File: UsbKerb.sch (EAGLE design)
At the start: 21 parts, among them IC1 XMEGA16A4A

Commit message: board Layout complete?
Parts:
- added C8: 470uf, rcl:CPOL-USG
- added U1: UA78M33CDCY, usb:UA78M33CDCY
- renumbered U$1 to U2
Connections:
- removed net N$15: JP2.3
- net +3V3: now also U1.INPUT
- net +5V: now also C8.+, U1.OUTPUT
- net GND: now also C8.-, U1.COM, U1.COM_2
- net N$18: now also JP2.3
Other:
- moved on the sheet: JP2
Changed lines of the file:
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@@
 <part name="U$3" library="usb" deviceset="TVS" device=""/>
 <part name="U$4" library="usb" deviceset="12MHZ" device=""/>
-<part name="U$1" library="usb" deviceset="3.3TVS" device=""/>
+<part name="U2" library="usb" deviceset="3.3TVS" device=""/>
 <part name="GND10" library="supply1" deviceset="GND" device=""/>
 <part name="C4" library="rcl" deviceset="C-EU" device="C0805K" value="18pf"/>
@@
 <part name="+3V4" library="supply1" deviceset="+3V3" device=""/>
 <part name="+3V5" library="supply1" deviceset="+3V3" device=""/>
+<part name="U1" library="usb" deviceset="UA78M33CDCY" device=""/>
+<part name="P+3" library="supply1" deviceset="+5V" device=""/>
+<part name="GND13" library="supply1" deviceset="GND" device=""/>
+<part name="C8" library="rcl" deviceset="CPOL-US" device="G" value="470uf"/>
 </parts>
 <sheets>
@@
 <instance part="U$3" gate="G$1" x="195.58" y="-15.24"/>
 <instance part="U$4" gate="G$1" x="15.24" y="30.48" rot="R90"/>
-<instance part="U$1" gate="G$1" x="99.06" y="-22.86"/>
+<instance part="U2" gate="G$1" x="99.06" y="-22.86"/>
 <instance part="GND10" gate="1" x="195.58" y="-27.94"/>
 <instance part="C4" gate="G$1" x="2.54" y="38.1" rot="R90"/>
@@
 <instance part="C6" gate="G$1" x="210.82" y="-12.7"/>
 <instance part="C7" gate="G$1" x="220.98" y="-12.7"/>
-<instance part="JP2" gate="A" x="48.26" y="-22.86"/>
+<instance part="JP2" gate="A" x="45.72" y="-22.86"/>
 <instance part="P+8" gate="1" x="35.56" y="-12.7"/>
 <instance part="GND12" gate="1" x="63.5" y="-15.24"/>
@@
 <instance part="+3V4" gate="G$1" x="81.28" y="-12.7"/>
 <instance part="+3V5" gate="G$1" x="25.4" y="71.12"/>
+<instance part="U1" gate="A" x="251.46" y="-7.62"/>
+<instance part="P+3" gate="1" x="297.18" y="-2.54"/>
+<instance part="GND13" gate="1" x="297.18" y="-27.94"/>
+<instance part="C8" gate="G$1" x="281.94" y="-12.7"/>
 </instances>
 <busses>
@@
 <wire x1="127" y1="-20.32" x2="127" y2="25.4" width="0.1524" layer="91"/>
 <junction x="127" y="25.4"/>
-<pinref part="U$1" gate="G$1" pin="2"/>
+<pinref part="U2" gate="G$1" pin="2"/>
 <wire x1="127" y1="-20.32" x2="111.76" y2="-20.32" width="0.1524" layer="91"/>
 </segment>
@@
 <wire x1="116.84" y1="-15.24" x2="116.84" y2="20.32" width="0.1524" layer="91"/>
 <junction x="116.84" y="20.32"/>
-<pinref part="U$1" gate="G$1" pin="1"/>
+<pinref part="U2" gate="G$1" pin="1"/>
 <wire x1="116.84" y1="-15.24" x2="111.76" y2="-15.24" width="0.1524" layer="91"/>
 </segment>
@@
 <wire x1="86.36" y1="-25.4" x2="81.28" y2="-25.4" width="0.1524" layer="91"/>
 <wire x1="81.28" y1="-25.4" x2="81.28" y2="-30.48" width="0.1524" layer="91"/>
-<pinref part="U$1" gate="G$1" pin="GND"/>
+<pinref part="U2" gate="G$1" pin="GND"/>
 </segment>
 <segment>
@@
 <wire x1="210.82" y1="-17.78" x2="210.82" y2="-22.86" width="0.1524" layer="91"/>
 <junction x="210.82" y="-22.86"/>
+<pinref part="U1" gate="A" pin="COM"/>
+<wire x1="220.98" y1="-22.86" x2="251.46" y2="-22.86" width="0.1524" layer="91"/>
+<wire x1="251.46" y1="-22.86" x2="254" y2="-22.86" width="0.1524" layer="91"/>
+<wire x1="254" y1="-22.86" x2="254" y2="-17.78" width="0.1524" layer="91"/>
+<junction x="220.98" y="-22.86"/>
+<pinref part="U1" gate="A" pin="COM_2"/>
+<wire x1="251.46" y1="-17.78" x2="251.46" y2="-22.86" width="0.1524" layer="91"/>
+<junction x="251.46" y="-22.86"/>
+<wire x1="254" y1="-22.86" x2="281.94" y2="-22.86" width="0.1524" layer="91"/>
+<wire x1="281.94" y1="-22.86" x2="297.18" y2="-22.86" width="0.1524" layer="91"/>
+<wire x1="297.18" y1="-22.86" x2="297.18" y2="-25.4" width="0.1524" layer="91"/>
+<junction x="254" y="-22.86"/>
+<pinref part="GND13" gate="1" pin="GND"/>
+<pinref part="C8" gate="G$1" pin="-"/>
+<wire x1="281.94" y1="-17.78" x2="281.94" y2="-22.86" width="0.1524" layer="91"/>
+<junction x="281.94" y="-22.86"/>
 </segment>
 <segment>
@@
 <segment>
 <pinref part="JP2" gate="A" pin="2"/>
-<wire x1="53.34" y1="-20.32" x2="58.42" y2="-20.32" width="0.1524" layer="91"/>
+<wire x1="50.8" y1="-20.32" x2="58.42" y2="-20.32" width="0.1524" layer="91"/>
 <wire x1="58.42" y1="-20.32" x2="58.42" y2="-12.7" width="0.1524" layer="91"/>
 <pinref part="GND12" gate="1" pin="GND"/>
@@
 <pinref part="JP2" gate="A" pin="1"/>
 <pinref part="P+8" gate="1" pin="+5V"/>
-<wire x1="45.72" y1="-20.32" x2="35.56" y2="-20.32" width="0.1524" layer="91"/>
+<wire x1="43.18" y1="-20.32" x2="35.56" y2="-20.32" width="0.1524" layer="91"/>
 <wire x1="35.56" y1="-20.32" x2="35.56" y2="-15.24" width="0.1524" layer="91"/>
+</segment>
+<segment>
+<pinref part="U1" gate="A" pin="OUTPUT"/>
+<pinref part="P+3" gate="1" pin="+5V"/>
+<wire x1="276.86" y1="-7.62" x2="281.94" y2="-7.62" width="0.1524" layer="91"/>
+<wire x1="281.94" y1="-7.62" x2="297.18" y2="-7.62" width="0.1524" layer="91"/>
+<wire x1="297.18" y1="-7.62" x2="297.18" y2="-5.08" width="0.1524" layer="91"/>
+<pinref part="C8" gate="G$1" pin="+"/>
+<wire x1="281.94" y1="-10.16" x2="281.94" y2="-7.62" width="0.1524" layer="91"/>
+<junction x="281.94" y="-7.62"/>
 </segment>
 </net>
@@
 <wire x1="22.86" y1="5.08" x2="22.86" y2="-25.4" width="0.1524" layer="91"/>
 <pinref part="JP2" gate="A" pin="5"/>
-<wire x1="22.86" y1="-25.4" x2="45.72" y2="-25.4" width="0.1524" layer="91"/>
+<wire x1="22.86" y1="-25.4" x2="43.18" y2="-25.4" width="0.1524" layer="91"/>
 </segment>
 </net>
 <net name="N$18" class="0">
 <segment>
-<pinref part="IC1" gate="G$1" pin="PD1"/>
-<wire x1="93.98" y1="15.24" x2="96.52" y2="15.24" width="0.1524" layer="91"/>
-<wire x1="96.52" y1="15.24" x2="96.52" y2="2.54" width="0.1524" layer="91"/>
 <wire x1="96.52" y1="2.54" x2="25.4" y2="2.54" width="0.1524" layer="91"/>
 <wire x1="25.4" y1="2.54" x2="25.4" y2="-22.86" width="0.1524" layer="91"/>
-</segment>
-</net>
-<net name="N$15" class="0">
-<segment>
 <pinref part="JP2" gate="A" pin="3"/>
-<wire x1="25.4" y1="-22.86" x2="45.72" y2="-22.86" width="0.1524" layer="91"/>
+<wire x1="43.18" y1="-22.86" x2="25.4" y2="-22.86" width="0.1524" layer="91"/>
+<wire x1="96.52" y1="2.54" x2="96.52" y2="15.24" width="0.1524" layer="91"/>
+<pinref part="IC1" gate="G$1" pin="PD1"/>
+<wire x1="96.52" y1="15.24" x2="93.98" y2="15.24" width="0.1524" layer="91"/>
 </segment>
 </net>
@@
 <wire x1="99.06" y1="0" x2="68.58" y2="0" width="0.1524" layer="91"/>
 <wire x1="68.58" y1="0" x2="68.58" y2="-22.86" width="0.1524" layer="91"/>
-<wire x1="68.58" y1="-22.86" x2="53.34" y2="-22.86" width="0.1524" layer="91"/>
+<wire x1="68.58" y1="-22.86" x2="50.8" y2="-22.86" width="0.1524" layer="91"/>
 <pinref part="JP2" gate="A" pin="4"/>
 </segment>
@@
 <wire x1="71.12" y1="-2.54" x2="71.12" y2="-25.4" width="0.1524" layer="91"/>
 <pinref part="JP2" gate="A" pin="6"/>
-<wire x1="71.12" y1="-25.4" x2="53.34" y2="-25.4" width="0.1524" layer="91"/>
+<wire x1="71.12" y1="-25.4" x2="50.8" y2="-25.4" width="0.1524" layer="91"/>
 </segment>
 </net>
@@
 <junction x="210.82" y="-7.62"/>
 <pinref part="+3V3" gate="G$1" pin="+3V3"/>
-</segment>
-<segment>
-<pinref part="U$1" gate="G$1" pin="VCC"/>
+<pinref part="U1" gate="A" pin="INPUT"/>
+<wire x1="220.98" y1="-7.62" x2="228.6" y2="-7.62" width="0.1524" layer="91"/>
+<junction x="220.98" y="-7.62"/>
+</segment>
+<segment>
+<pinref part="U2" gate="G$1" pin="VCC"/>
 <wire x1="86.36" y1="-20.32" x2="81.28" y2="-20.32" width="0.1524" layer="91"/>
 <wire x1="81.28" y1="-20.32" x2="81.28" y2="-15.24" width="0.1524" layer="91"/>

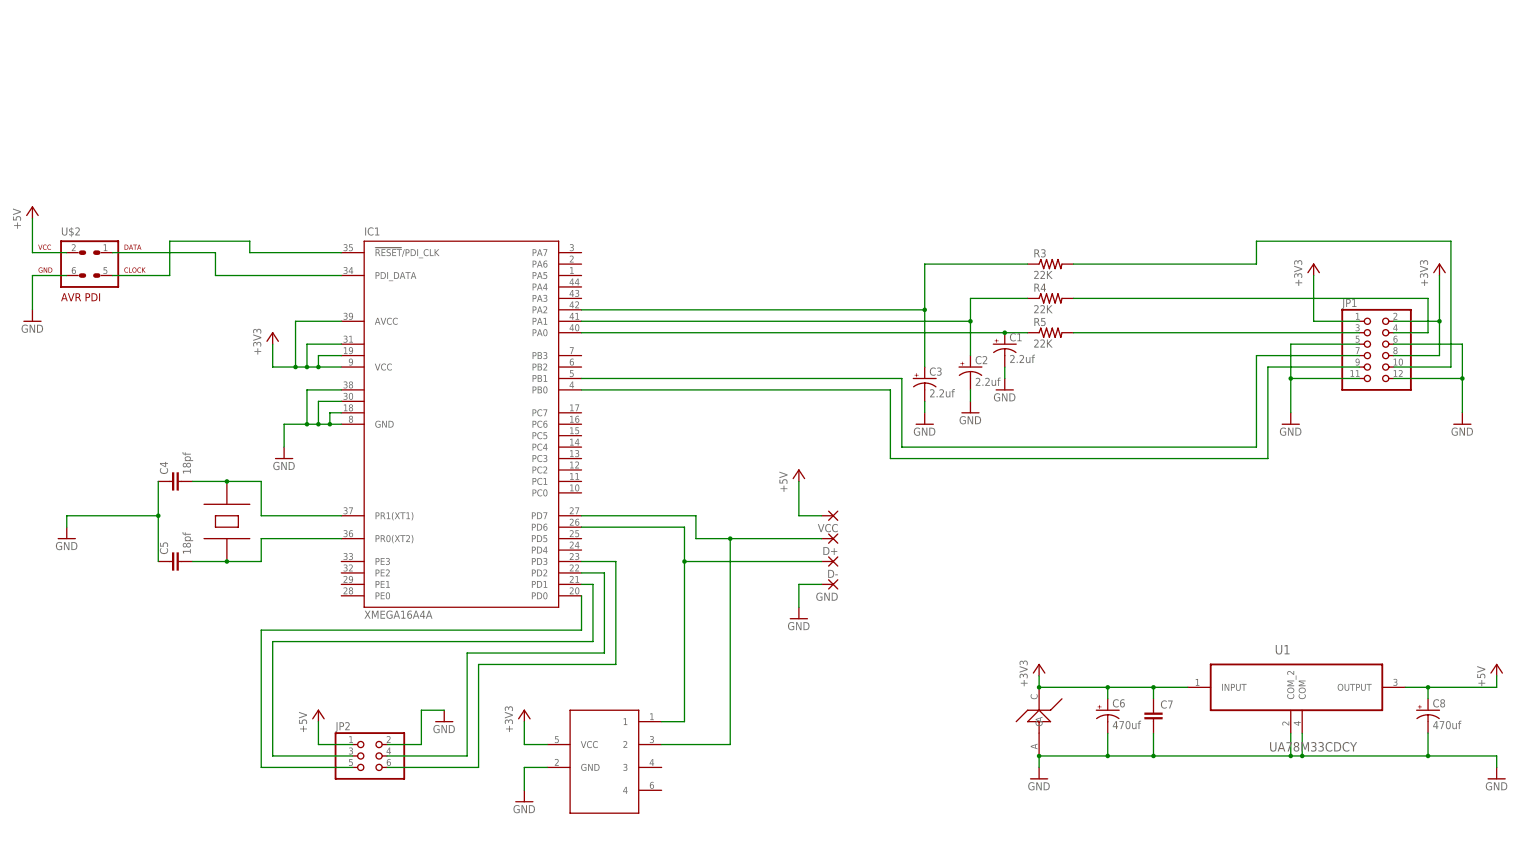
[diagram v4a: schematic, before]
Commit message: Corrected board layout for voltage and regulator footprint
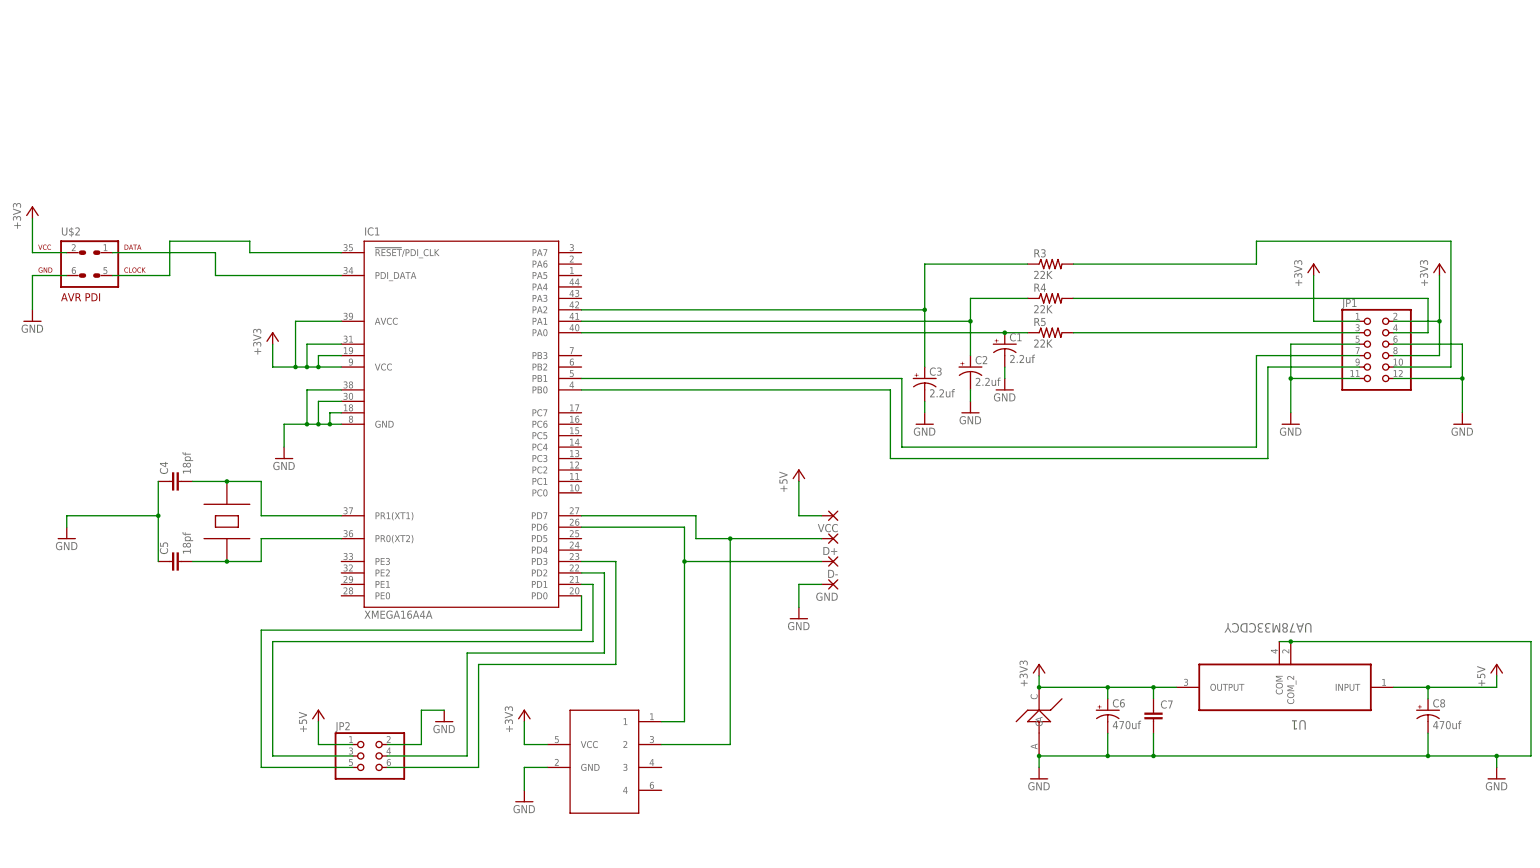
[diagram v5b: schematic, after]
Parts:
- C7: device rcl:C-EUC0805K -> resistor:C-EUC1206K
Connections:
- net +3V3: now also U$2.2, U1.OUTPUT; no longer U1.INPUT
- net +5V: now also U1.INPUT; no longer U$2.2, U1.OUTPUT
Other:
- moved on the sheet: U1
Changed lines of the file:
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@@
 <?xml version="1.0" encoding="utf-8"?>
 <!DOCTYPE eagle SYSTEM "eagle.dtd">
-<eagle version="7.1.0">
+<eagle version="7.2.0">
 <drawing>
 <settings>
@@
 <part name="GND8" library="supply1" deviceset="GND" device=""/>
 <part name="P+1" library="supply1" deviceset="+5V" device=""/>
-<part name="P+2" library="supply1" deviceset="+5V" device=""/>
 <part name="C1" library="resistor" deviceset="CPOL-US" device="B" value="2.2uf"/>
 <part name="C2" library="resistor" deviceset="CPOL-US" device="B" value="2.2uf"/>
@@
 <part name="GND11" library="supply1" deviceset="GND" device=""/>
 <part name="C6" library="rcl" deviceset="CPOL-US" device="G" value="470uf"/>
-<part name="C7" library="rcl" deviceset="C-EU" device="C0805K"/>
 <part name="JP2" library="pinhead" deviceset="PINHD-2X3" device=""/>
 <part name="P+8" library="supply1" deviceset="+5V" device=""/>
@@
 <part name="GND13" library="supply1" deviceset="GND" device=""/>
 <part name="C8" library="rcl" deviceset="CPOL-US" device="G" value="470uf"/>
+<part name="+3V6" library="supply1" deviceset="+3V3" device=""/>
+<part name="C7" library="resistor" deviceset="C-EU" device="C1206K"/>
 </parts>
 <sheets>
@@
 <instance part="GND8" gate="1" x="27.94" y="43.18"/>
 <instance part="P+1" gate="1" x="142.24" y="40.64"/>
-<instance part="P+2" gate="1" x="-27.94" y="99.06"/>
 <instance part="C1" gate="G$1" x="187.96" y="68.58"/>
 <instance part="C2" gate="G$1" x="180.34" y="63.5"/>
@@
 <instance part="GND11" gate="1" x="-20.32" y="25.4"/>
 <instance part="C6" gate="G$1" x="210.82" y="-12.7"/>
-<instance part="C7" gate="G$1" x="220.98" y="-12.7"/>
 <instance part="JP2" gate="A" x="45.72" y="-22.86"/>
 <instance part="P+8" gate="1" x="35.56" y="-12.7"/>
@@
 <instance part="+3V4" gate="G$1" x="81.28" y="-12.7"/>
 <instance part="+3V5" gate="G$1" x="25.4" y="71.12"/>
-<instance part="U1" gate="A" x="251.46" y="-7.62"/>
+<instance part="U1" gate="A" x="251.46" y="-7.62" rot="R180"/>
 <instance part="P+3" gate="1" x="297.18" y="-2.54"/>
 <instance part="GND13" gate="1" x="297.18" y="-27.94"/>
 <instance part="C8" gate="G$1" x="281.94" y="-12.7"/>
+<instance part="+3V6" gate="G$1" x="-27.94" y="99.06"/>
+<instance part="C7" gate="G$1" x="220.98" y="-12.7"/>
 </instances>
 <busses>
@@
 <pinref part="GND10" gate="1" pin="GND"/>
 <wire x1="195.58" y1="-22.86" x2="195.58" y2="-25.4" width="0.1524" layer="91"/>
-<pinref part="C7" gate="G$1" pin="2"/>
 <wire x1="220.98" y1="-17.78" x2="220.98" y2="-22.86" width="0.1524" layer="91"/>
 <wire x1="220.98" y1="-22.86" x2="210.82" y2="-22.86" width="0.1524" layer="91"/>
@@
 <wire x1="210.82" y1="-17.78" x2="210.82" y2="-22.86" width="0.1524" layer="91"/>
 <junction x="210.82" y="-22.86"/>
-<pinref part="U1" gate="A" pin="COM"/>
-<wire x1="220.98" y1="-22.86" x2="251.46" y2="-22.86" width="0.1524" layer="91"/>
-<wire x1="251.46" y1="-22.86" x2="254" y2="-22.86" width="0.1524" layer="91"/>
-<wire x1="254" y1="-22.86" x2="254" y2="-17.78" width="0.1524" layer="91"/>
+<wire x1="220.98" y1="-22.86" x2="281.94" y2="-22.86" width="0.1524" layer="91"/>
 <junction x="220.98" y="-22.86"/>
-<pinref part="U1" gate="A" pin="COM_2"/>
-<wire x1="251.46" y1="-17.78" x2="251.46" y2="-22.86" width="0.1524" layer="91"/>
-<junction x="251.46" y="-22.86"/>
-<wire x1="254" y1="-22.86" x2="281.94" y2="-22.86" width="0.1524" layer="91"/>
 <wire x1="281.94" y1="-22.86" x2="297.18" y2="-22.86" width="0.1524" layer="91"/>
 <wire x1="297.18" y1="-22.86" x2="297.18" y2="-25.4" width="0.1524" layer="91"/>
-<junction x="254" y="-22.86"/>
 <pinref part="GND13" gate="1" pin="GND"/>
 <pinref part="C8" gate="G$1" pin="-"/>
 <wire x1="281.94" y1="-17.78" x2="281.94" y2="-22.86" width="0.1524" layer="91"/>
 <junction x="281.94" y="-22.86"/>
+<pinref part="U1" gate="A" pin="COM"/>
+<pinref part="U1" gate="A" pin="COM_2"/>
+<wire x1="248.92" y1="2.54" x2="251.46" y2="2.54" width="0.1524" layer="91"/>
+<wire x1="251.46" y1="2.54" x2="304.8" y2="2.54" width="0.1524" layer="91"/>
+<wire x1="304.8" y1="2.54" x2="304.8" y2="-22.86" width="0.1524" layer="91"/>
+<junction x="251.46" y="2.54"/>
+<wire x1="304.8" y1="-22.86" x2="297.18" y2="-22.86" width="0.1524" layer="91"/>
+<junction x="297.18" y="-22.86"/>
+<pinref part="C7" gate="G$1" pin="2"/>
 </segment>
 <segment>
@@
 <net name="+5V" class="0">
 <segment>
-<pinref part="P+2" gate="1" pin="+5V"/>
-<wire x1="-27.94" y1="88.9" x2="-27.94" y2="96.52" width="0.1524" layer="91"/>
-<pinref part="U$2" gate="G$1" pin="2"/>
-<wire x1="-27.94" y1="88.9" x2="-20.32" y2="88.9" width="0.1524" layer="91"/>
-</segment>
-<segment>
 <pinref part="VCC" gate="1" pin="P"/>
 <pinref part="P+1" gate="1" pin="+5V"/>
@@
 </segment>
 <segment>
-<pinref part="U1" gate="A" pin="OUTPUT"/>
 <pinref part="P+3" gate="1" pin="+5V"/>
-<wire x1="276.86" y1="-7.62" x2="281.94" y2="-7.62" width="0.1524" layer="91"/>
 <wire x1="281.94" y1="-7.62" x2="297.18" y2="-7.62" width="0.1524" layer="91"/>
 <wire x1="297.18" y1="-7.62" x2="297.18" y2="-5.08" width="0.1524" layer="91"/>
@@
 <wire x1="281.94" y1="-10.16" x2="281.94" y2="-7.62" width="0.1524" layer="91"/>
 <junction x="281.94" y="-7.62"/>
+<pinref part="U1" gate="A" pin="INPUT"/>
+<wire x1="281.94" y1="-7.62" x2="274.32" y2="-7.62" width="0.1524" layer="91"/>
 </segment>
 </net>
@@
 <pinref part="U$3" gate="G$1" pin="C"/>
 <wire x1="195.58" y1="-7.62" x2="195.58" y2="-5.08" width="0.1524" layer="91"/>
-<pinref part="C7" gate="G$1" pin="1"/>
 <wire x1="220.98" y1="-10.16" x2="220.98" y2="-7.62" width="0.1524" layer="91"/>
 <wire x1="220.98" y1="-7.62" x2="210.82" y2="-7.62" width="0.1524" layer="91"/>
@@
 <junction x="210.82" y="-7.62"/>
 <pinref part="+3V3" gate="G$1" pin="+3V3"/>
-<pinref part="U1" gate="A" pin="INPUT"/>
-<wire x1="220.98" y1="-7.62" x2="228.6" y2="-7.62" width="0.1524" layer="91"/>
 <junction x="220.98" y="-7.62"/>
+<pinref part="U1" gate="A" pin="OUTPUT"/>
+<wire x1="220.98" y1="-7.62" x2="226.06" y2="-7.62" width="0.1524" layer="91"/>
+<pinref part="C7" gate="G$1" pin="1"/>
 </segment>
 <segment>
@@
 <pinref part="+3V5" gate="G$1" pin="+3V3"/>
 </segment>
-</net>
+<segment>
+<wire x1="-27.94" y1="88.9" x2="-27.94" y2="96.52" width="0.1524" layer="91"/>
+<pinref part="U$2" gate="G$1" pin="2"/>
+<wire x1="-27.94" y1="88.9" x2="-20.32" y2="88.9" width="0.1524" layer="91"/>
+<pinref part="+3V6" gate="G$1" pin="+3V3"/>
+</segment>
+</net>
